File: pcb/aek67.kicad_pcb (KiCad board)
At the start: 2 copper layers, 154 parts, among them J1 AVR-ISP-6, K1 K_GRV, K10 K_LAPP, K11 K_2, K12 K_W, K13 K_S, K14 K_X, K15 K_LALT, K16 K_3, K17 K_E, K18 K_D, K19 K_C, K2 K_TAB, K20 K_4, K21 K_R, K22 K_F, K23 K_V, K24 K_5, K25 K_T, K26 K_G, K27 K_B, K28 K_SPC, K29 K_6, K3 K_CAPS_LOCK, K30 K_Y, K31 K_H, K32 K_N, K33 K_7, K34 K_U, K35 K_J, K36 K_M, K37 K_8, K38 K_I, K39 K_K, K4 K_LSHIFT, K40 K_COMMA, K41 K_9, K42 K_O, K43 K_L, K44 K_DOT, K45 K_0, K46 K_P, K47 K_SEMIC, K48 K_SLASH, K49 K_RALT, K5 K_LCTRL, K50 K_MINUS, K51 K_LBRC, K52 K_QUOTE, K53 K_RAPP, K54 K_EQUAL, K55 K_RBRC, K56 K_ENTER, K57 K_RSHIFT, K58 K_LEFT, K59 K_BACKSPACE, K6 K_1, K60 K_BSLSH, K61 K_UP, K62 K_DOWN, K63 K_PAGE_UP, K64 K_PAGE_DN, K65 K_INSERT, K66 K_DELETE, K67 K_RIGHT, K7 K_Q, K8 K_A, K9 K_Z, SW1 SW_PUSH, U1 PRTR5V0U2X, U2 ATmega32U4-AU, X1 XTAL_GND

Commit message: USB connector & cut lines
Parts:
- C1, C2, C3, C4, C5, C6, C7, F1, R1, R2, R3, R4, R5, R6, SW1, U1, U2, USB1, X1: moved to B.Cu
- moved R6 234.7 mm to (225.0, 110.0), turned to 90 degrees
- moved F1 233.6 mm to (176.9, 33.0), turned to 270 degrees
- moved USB1 230.4 mm to (172.9, 15.1)
- moved U2 228.6 mm to (215.0, 105.0)
- moved R5 226.7 mm to (172.9, 32.9), turned to 90 degrees
- moved R2 217.4 mm to (169.0, 27.5), turned to 90 degrees
- moved U1 215.7 mm to (173.0, 27.5), turned to 90 degrees
- moved SW1 215.6 mm to (195.0, 105.0), turned to 180 degrees
- moved R1 215.0 mm to (177.0, 27.5), turned to 90 degrees
- moved R4 211.8 mm to (169.5, 32.9), turned to 90 degrees
- moved C6 208.8 mm to (220.0, 120.0), turned to 270 degrees
- moved C5 206.2 mm to (210.0, 120.0), turned to 270 degrees
- moved C3 205.1 mm to (202.5, 100.0)
- moved X1 202.8 mm to (215.0, 120.0)
- moved C7 202.0 mm to (202.5, 115.0), turned to 180 degrees
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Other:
- board outline added: 304.8 x 100.4 mm

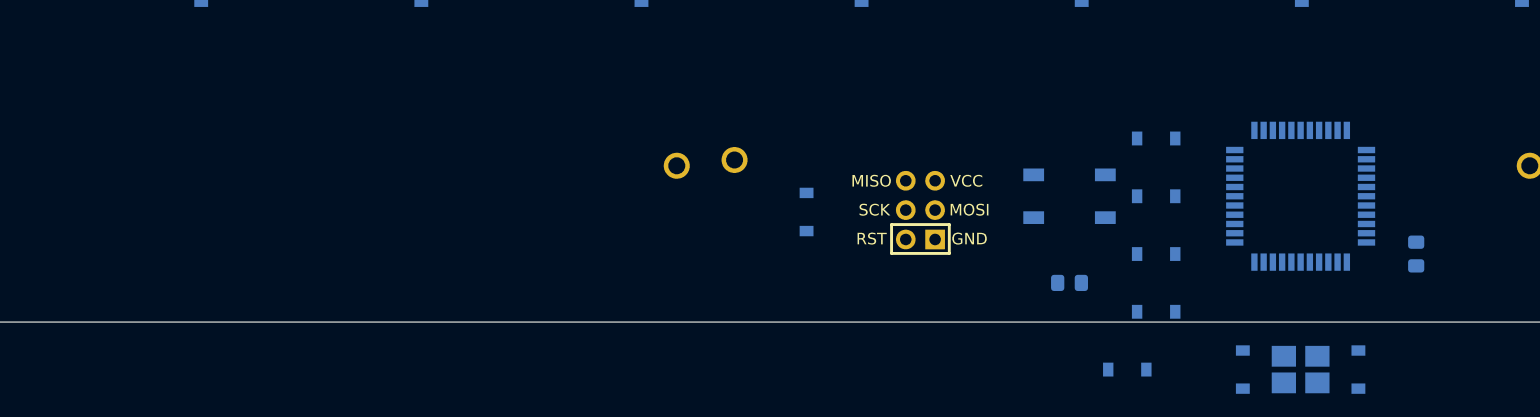
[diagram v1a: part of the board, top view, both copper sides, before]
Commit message: position all elements inside PCB
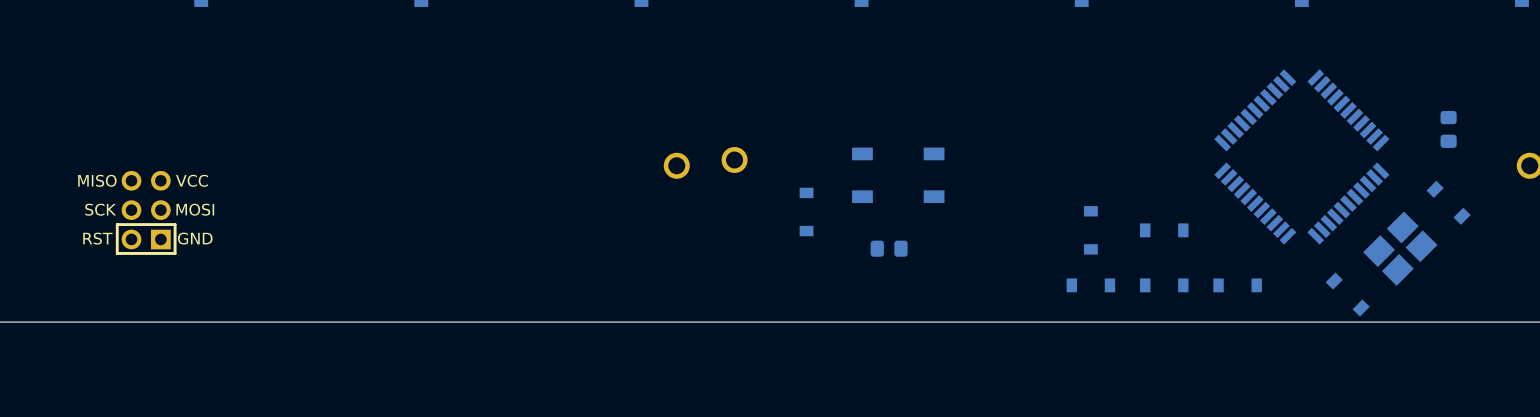
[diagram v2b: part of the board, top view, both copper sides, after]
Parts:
- moved J1 67.0 mm to (115.1, 106.2)
- moved C6 16.4 mm to (227.8, 105.6), turned to 315 degrees
- moved R3 15.9 mm to (179.4, 109.5)
- moved SW1 14.9 mm to (180.2, 103.2)
- moved C3 13.9 mm to (196.8, 112.7)
- moved X1 13.6 mm to (223.6, 109.5), turned to 45 degrees
- moved C1 12.5 mm to (196.8, 108.0), turned to 90 degrees
- moved C5 11.2 mm to (219.1, 113.5), turned to 315 degrees
- moved R6 11.1 mm to (227.8, 99.2)
- moved C7 7.41 mm to (209.6, 112.7)
- moved U2 3.40 mm to (215.1, 101.6), turned to 45 degrees
- moved C2 3.03 mm to (203.2, 108.0)
- moved C4 2.80 mm to (203.2, 112.7)

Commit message: routed switches vertical & diodes
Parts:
- moved J1 31.8 mm to (146.8, 106.4)
- moved C6 24.2 mm to (204.5, 99.0), turned to 135 degrees
- moved C5 22.9 mm to (212.0, 91.8), turned to 135 degrees
- moved X1 21.0 mm to (208.2, 95.2), turned to 225 degrees
- moved R3 10.9 mm to (189.8, 106.2), turned to 270 degrees
- moved R6 8.33 mm to (230.0, 107.2)
- moved C1 8.09 mm to (190.0, 112.2), turned to 270 degrees
- moved C2 6.94 mm to (197.8, 112.2), turned to 270 degrees
- moved R4 6.65 mm to (174.4, 37.4)
- moved R5 4.71 mm to (171.5, 37.4)
- moved U2 4.63 mm to (218.5, 104.8)
- moved C7 4.32 mm to (205.2, 112.2), turned to 270 degrees
- moved U1 4.00 mm to (172.8, 31.5), turned to 270 degrees
- moved SW1 3.70 mm to (182.2, 106.2)
- moved C3 2.89 mm to (194.0, 112.2), turned to 270 degrees
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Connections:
- C1 pad 2: +5V -> GND
- C2 pad 2: +5V -> GND
- C3 pad 2: +5V -> GND
- C4 pad 2: +5V -> GND
- C5 pad 2: Net-(C5-Pad2) -> GND
- C6 pad 2: Net-(C5-Pad2) -> GND
- C7 pad 2: +5V -> GND
- J1 pad 6: +5V -> GND
- K53 pad 1: Net-(K53-Pad1) -> col11
- R1 pad 1: +5V -> GND
- R2 pad 2: +5V -> GND
- R6 pad 1: +5V -> GND
- U1 pad 1: +5V -> GND
- U2 pad 15: +5V -> GND
- U2 pad 23: +5V -> GND
- U2 pad 35: +5V -> GND
- U2 pad 43: +5V -> GND
- U2 pad 5: +5V -> GND
- USB1 pad 1: +5V -> GND
- USB1 pad 12: +5V -> GND
- USB1 pad 13: +5V -> GND
- X1 pad 3: Net-(C5-Pad2) -> GND
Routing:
- net GND: track 0.00 -> 178.0 mm
- net col5: track 0.00 -> 100.4 mm
- net col12: track 0.00 -> 97.8 mm
- net SCLK: track 0.00 -> 94.1 mm
- net Net-(R5-Pad1): track 0.00 -> 92.5 mm
- net Net-(R4-Pad1): track 0.00 -> 91.6 mm
- net col2: track 0.00 -> 90.3 mm
- net col10: track 0.00 -> 89.0 mm
- net +5V: track 0.00 -> 84.7 mm, vias 0 -> 12
- net col13: track 0.00 -> 84.5 mm
- net col0: track 0.00 -> 84.1 mm
- net col11: track 0.00 -> 83.8 mm
- net col14: track 0.00 -> 77.1 mm
- net col4: track 0.00 -> 69.4 mm
- net col3: track 0.00 -> 68.1 mm
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- added copper zone on B.Cu, net GND
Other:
- net class Power added: clearance 0.2, trace_width 0.381, via_dia 0.8, via_drill 0.4

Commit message: row0
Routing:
- net row0: track 0.00 -> 347.2 mm, vias 0 -> 16
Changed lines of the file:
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@@
     (thickness 1.6)
     (drawings 14)
-    (tracks 534)
+    (tracks 613)
     (zones 0)
     (modules 154)
@@
   (segment (start 35.5125 28.5125) (end 38.1 28.5125) (width 0.25) (layer B.Cu) (net 5))
   (segment (start 32.6625 25.6625) (end 35.5125 28.5125) (width 0.25) (layer B.Cu) (net 5))
+  (segment (start 36.5 33.2625) (end 36.5 34.75) (width 0.25) (layer B.Cu) (net 6))
+  (segment (start 37.95 31.8125) (end 36.5 33.2625) (width 0.25) (layer B.Cu) (net 6))
+  (via (at 36.5 34.75) (size 0.8) (drill 0.4) (layers F.Cu B.Cu) (net 6))
+  (segment (start 38.1 31.8125) (end 37.95 31.8125) (width 0.25) (layer B.Cu) (net 6))
+  (via (at 56.25 34.75) (size 0.8) (drill 0.4) (layers F.Cu B.Cu) (net 6))
+  (segment (start 36.5 34.75) (end 56.25 34.75) (width 0.25) (layer F.Cu) (net 6))
+  (segment (start 57.09375 31.8125) (end 57.94375 31.8125) (width 0.25) (layer B.Cu) (net 6))
+  (segment (start 56.25 32.65625) (end 57.09375 31.8125) (width 0.25) (layer B.Cu) (net 6))
+  (segment (start 56.25 34.75) (end 56.25 32.65625) (width 0.25) (layer B.Cu) (net 6))
+  (via (at 74.75 34.75) (size 0.8) (drill 0.4) (layers F.Cu B.Cu) (net 6))
+  (segment (start 56.25 34.75) (end 74.75 34.75) (width 0.25) (layer F.Cu) (net 6))
+  (segment (start 76.14375 31.8125) (end 76.99375 31.8125) (width 0.25) (layer B.Cu) (net 6))
+  (segment (start 74.75 33.20625) (end 76.14375 31.8125) (width 0.25) (layer B.Cu) (net 6))
+  (segment (start 74.75 34.75) (end 74.75 33.20625) (width 0.25) (layer B.Cu) (net 6))
+  (via (at 94 34.75) (size 0.8) (drill 0.4) (layers F.Cu B.Cu) (net 6))
+  (segment (start 74.75 34.75) (end 94 34.75) (width 0.25) (layer F.Cu) (net 6))
+  (segment (start 95.19375 31.8125) (end 96.04375 31.8125) (width 0.25) (layer B.Cu) (net 6))
+  (segment (start 94 33.00625) (end 95.19375 31.8125) (width 0.25) (layer B.Cu) (net 6))
+  (segment (start 94 34.75) (end 94 33.00625) (width 0.25) (layer B.Cu) (net 6))
+  (segment (start 94 34.75) (end 112.5 34.75) (width 0.25) (layer F.Cu) (net 6))
+  (segment (start 112.5 34.75) (end 112.75 34.75) (width 0.25) (layer F.Cu) (net 6))
+  (via (at 112.5 34.75) (size 0.8) (drill 0.4) (layers F.Cu B.Cu) (net 6))
+  (segment (start 112.5 34.75) (end 112.5 32.75) (width 0.25) (layer B.Cu) (net 6))
+  (segment (start 113.4375 31.8125) (end 115.09375 31.8125) (width 0.25) (layer B.Cu) (net 6))
+  (segment (start 112.5 32.75) (end 113.4375 31.8125) (width 0.25) (layer B.Cu) (net 6))
+  (via (at 131.25 34.75) (size 0.8) (drill 0.4) (layers F.Cu B.Cu) (net 6))
+  (segment (start 112.5 34.75) (end 131.25 34.75) (width 0.25) (layer F.Cu) (net 6))
+  (segment (start 131.25 34.75) (end 131.25 33.5) (width 0.25) (layer B.Cu) (net 6))
+  (segment (start 132.9375 31.8125) (end 134.14375 31.8125) (width 0.25) (layer B.Cu) (net 6))
+  (segment (start 131.25 33.5) (end 132.9375 31.8125) (width 0.25) (layer B.Cu) (net 6))
+  (via (at 150.5 34.75) (size 0.8) (drill 0.4) (layers F.Cu B.Cu) (net 6))
+  (segment (start 131.25 34.75) (end 150.5 34.75) (width 0.25) (layer F.Cu) (net 6))
+  (segment (start 150.5 34.75) (end 150.5 32.75) (width 0.25) (layer B.Cu) (net 6))
+  (segment (start 151.4375 31.8125) (end 153.19375 31.8125) (width 0.25) (layer B.Cu) (net 6))
+  (segment (start 150.5 32.75) (end 151.4375 31.8125) (width 0.25) (layer B.Cu) (net 6))
+  (segment (start 153.19375 31.8125) (end 156.5 31.8125) (width 0.25) (layer B.Cu) (net 6))
+  (segment (start 156.5 31.8125) (end 157.8125 31.8125) (width 0.25) (layer B.Cu) (net 6))
+  (segment (start 157.8125 31.8125) (end 158.75 32.75) (width 0.25) (layer B.Cu) (net 6))
+  (segment (start 158.75 32.75) (end 158.75 34.75) (width 0.25) (layer B.Cu) (net 6))
+  (via (at 158.75 34.75) (size 0.8) (drill 0.4) (layers F.Cu B.Cu) (net 6))
+  (via (at 188.25 34.75) (size 0.8) (drill 0.4) (layers F.Cu B.Cu) (net 6))
+  (segment (start 158.75 34.75) (end 188.25 34.75) (width 0.25) (layer F.Cu) (net 6))
+  (segment (start 188.25 34.75) (end 188.25 32.75) (width 0.25) (layer B.Cu) (net 6))
+  (segment (start 189.35 31.65) (end 191 31.65) (width 0.25) (layer B.Cu) (net 6))
+  (segment (start 188.25 32.75) (end 189.35 31.65) (width 0.25) (layer B.Cu) (net 6))
+  (segment (start 188.25 34.75) (end 207.5 34.75) (width 0.25) (layer F.Cu) (net 6))
+  (via (at 207.5 34.75) (size 0.8) (drill 0.4) (layers F.Cu B.Cu) (net 6))
+  (segment (start 207.5 34.75) (end 207.5 33.25) (width 0.25) (layer B.Cu) (net 6))
+  (segment (start 208.9375 31.8125) (end 210.34375 31.8125) (width 0.25) (layer B.Cu) (net 6))
+  (segment (start 207.5 33.25) (end 208.9375 31.8125) (width 0.25) (layer B.Cu) (net 6))
+  (segment (start 207.5 34.75) (end 224 34.75) (width 0.25) (layer F.Cu) (net 6))
+  (segment (start 224 34.75) (end 226 34.75) (width 0.25) (layer F.Cu) (net 6))
+  (via (at 226 34.75) (size 0.8) (drill 0.4) (layers F.Cu B.Cu) (net 6))
+  (segment (start 227.4375 31.8125) (end 229.39375 31.8125) (width 0.25) (layer B.Cu) (net 6))
+  (segment (start 226 33.25) (end 227.4375 31.8125) (width 0.25) (layer B.Cu) (net 6))
+  (segment (start 226 34.75) (end 226 33.25) (width 0.25) (layer B.Cu) (net 6))
+  (segment (start 226 34.75) (end 242.25 34.75) (width 0.25) (layer F.Cu) (net 6))
+  (segment (start 242.25 34.75) (end 246 34.75) (width 0.25) (layer F.Cu) (net 6))
+  (via (at 246 34.75) (size 0.8) (drill 0.4) (layers F.Cu B.Cu) (net 6))
+  (via (at 246 34.75) (size 0.8) (drill 0.4) (layers F.Cu B.Cu) (net 6))
+  (segment (start 246 34.184315) (end 246 34.75) (width 0.25) (layer B.Cu) (net 6))
+  (segment (start 246 33.40625) (end 246 34.184315) (width 0.25) (layer B.Cu) (net 6))
+  (segment (start 247.59375 31.8125) (end 246 33.40625) (width 0.25) (layer B.Cu) (net 6))
+  (segment (start 248.44375 31.8125) (end 247.59375 31.8125) (width 0.25) (layer B.Cu) (net 6))
+  (via (at 265 34.75) (size 0.8) (drill 0.4) (layers F.Cu B.Cu) (net 6))
+  (segment (start 246 34.75) (end 265 34.75) (width 0.25) (layer F.Cu) (net 6))
+  (segment (start 265 34.75) (end 265 33.25) (width 0.25) (layer B.Cu) (net 6))
+  (segment (start 266.4375 31.8125) (end 267.49375 31.8125) (width 0.25) (layer B.Cu) (net 6))
+  (segment (start 265 33.25) (end 266.4375 31.8125) (width 0.25) (layer B.Cu) (net 6))
+  (segment (start 265 34.75) (end 295 34.75) (width 0.25) (layer F.Cu) (net 6))
+  (via (at 295 34.75) (size 0.8) (drill 0.4) (layers F.Cu B.Cu) (net 6))
+  (segment (start 295 34.75) (end 295 33.25) (width 0.25) (layer B.Cu) (net 6))
+  (segment (start 296.4375 31.8125) (end 297.65625 31.8125) (width 0.25) (layer B.Cu) (net 6))
+  (segment (start 295 33.25) (end 296.4375 31.8125) (width 0.25) (layer B.Cu) (net 6))
+  (segment (start 295 34.75) (end 316 34.75) (width 0.25) (layer F.Cu) (net 6))
+  (via (at 317.5 33.25) (size 0.8) (drill 0.4) (layers F.Cu B.Cu) (net 6))
+  (segment (start 316 34.75) (end 317.5 33.25) (width 0.25) (layer F.Cu) (net 6))
+  (segment (start 322.1125 33.25) (end 322.2625 33.4) (width 0.25) (layer B.Cu) (net 6))
+  (segment (start 317.5 33.25) (end 322.1125 33.25) (width 0.25) (layer B.Cu) (net 6))
   (segment (start 43.65625 46.8625) (end 43.65625 47.5625) (width 0.25) (layer B.Cu) (net 7))
   (segment (start 41.50625 44.7125) (end 43.65625 46.8625) (width 0.25) (layer B.Cu) (net 7))

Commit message: re-annotated everything in line instead of column
which is more clear for the matrix
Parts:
- renumbered D41 to D10, D45 to D11, D50 to D12, D54 to D13, D59 to D14, D63 to D15, D2 to D16, D7 to D17, D12 to D18, D17 to D19, D6 to D2, D21 to D20, D25 to D21, D30 to D22, D34 to D23, D38 to D24, D42 to D25, D46 to D26, D51 to D27, D55 to D28, D60 to D29, D11 to D3, D64 to D30, D3 to D31, D8 to D32, D13 to D33, D18 to D34, D22 to D35, D26 to D36, D31 to D37, D35 to D38, D16 to D4, D43 to D40, D47 to D41, D52 to D42, D56 to D43, D65 to D44, D4 to D45, D9 to D46, D14 to D47, D19 to D48, D23 to D49, D20 to D5, D27 to D50, D32 to D51, D36 to D52, D40 to D53, D44 to D54, D48 to D55, D57 to D56, D61 to D57, D66 to D58, D5 to D59, D24 to D6, D10 to D60, D15 to D61, D28 to D62, D49 to D63, D53 to D64, D58 to D65, D62 to D66, D29 to D7, D33 to D8, D37 to D9, K41 to K10, K45 to K11, K50 to K12, K54 to K13, K59 to K14, K63 to K15, K2 to K16, K7 to K17, K12 to K18, K17 to K19, K6 to K2, K21 to K20, K25 to K21, K30 to K22, K34 to K23, K38 to K24, K42 to K25, K46 to K26, K51 to K27, K55 to K28, K60 to K29, K11 to K3, K64 to K30, K3 to K31, K8 to K32, K13 to K33, K18 to K34, K22 to K35, K26 to K36, K31 to K37, K35 to K38, K16 to K4, K43 to K40, K47 to K41, K52 to K42, K56 to K43, K65 to K44, K4 to K45, K9 to K46, K14 to K47, K19 to K48, K23 to K49, K20 to K5, K27 to K50, K32 to K51, K36 to K52, K40 to K53, K44 to K54, K48 to K55, K57 to K56, K61 to K57, K66 to K58, K5 to K59, K24 to K6, K10 to K60, K15 to K61, K28 to K62, K49 to K63, K53 to K64, K58 to K65, K62 to K66, K29 to K7, K33 to K8, K37 to K9, R3 to R1, R4 to R2, R5 to R3, R6 to R4, R1 to R5, R2 to R6, U2 to U1, U1 to U2

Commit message: row1
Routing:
- net row1: track 0.00 -> 405.2 mm, vias 0 -> 15
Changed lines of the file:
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@@
     (thickness 1.6)
     (drawings 14)
-    (tracks 613)
+    (tracks 701)
     (zones 0)
     (modules 154)
     (nets 110)
   )
-  (page A4)
+  (page A3)
   (layers
     (0 F.Cu signal)
@@
   (segment (start 55.79375 25.6625) (end 57.94375 27.8125) (width 0.25) (layer B.Cu) (net 7))
   (segment (start 51.7125 25.6625) (end 55.79375 25.6625) (width 0.25) (layer B.Cu) (net 7))
+  (segment (start 42.80625 50.8625) (end 41 52.66875) (width 0.25) (layer B.Cu) (net 8))
+  (segment (start 43.65625 50.8625) (end 42.80625 50.8625) (width 0.25) (layer B.Cu) (net 8))
+  (via (at 41 57.5) (size 0.8) (drill 0.4) (layers F.Cu B.Cu) (net 8))
+  (via (at 64.5 57.5) (size 0.8) (drill 0.4) (layers F.Cu B.Cu) (net 8))
+  (segment (start 41 57.5) (end 64.5 57.5) (width 0.25) (layer F.Cu) (net 8))
+  (segment (start 65.8875 50.8625) (end 67.46875 50.8625) (width 0.25) (layer B.Cu) (net 8))
+  (segment (start 64.5 52.25) (end 65.8875 50.8625) (width 0.25) (layer B.Cu) (net 8))
+  (via (at 83.75 57.5) (size 0.8) (drill 0.4) (layers F.Cu B.Cu) (net 8))
+  (segment (start 64.5 57.5) (end 83.75 57.5) (width 0.25) (layer F.Cu) (net 8))
+  (segment (start 84.8875 50.8625) (end 86.51875 50.8625) (width 0.25) (layer B.Cu) (net 8))
+  (segment (start 83.75 52) (end 84.8875 50.8625) (width 0.25) (layer B.Cu) (net 8))
+  (segment (start 83.75 57.5) (end 103 57.5) (width 0.25) (layer F.Cu) (net 8))
+  (via (at 103 57.5) (size 0.8) (drill 0.4) (layers F.Cu B.Cu) (net 8))
+  (segment (start 104.3875 50.8625) (end 105.56875 50.8625) (width 0.25) (layer B.Cu) (net 8))
+  (segment (start 103 52.25) (end 104.3875 50.8625) (width 0.25) (layer B.Cu) (net 8))
+  (segment (start 103 57.5) (end 121 57.5) (width 0.25) (layer F.Cu) (net 8))
+  (via (at 121 57.5) (size 0.8) (drill 0.4) (layers F.Cu B.Cu) (net 8))
+  (segment (start 122.6375 50.8625) (end 124.61875 50.8625) (width 0.25) (layer B.Cu) (net 8))
+  (segment (start 121 52.5) (end 122.6375 50.8625) (width 0.25) (layer B.Cu) (net 8))
+  (via (at 139.75 57.5) (size 0.8) (drill 0.4) (layers F.Cu B.Cu) (net 8))
+  (segment (start 121 57.5) (end 139.75 57.5) (width 0.25) (layer F.Cu) (net 8))
+  (segment (start 141.3875 50.8625) (end 143.66875 50.8625) (width 0.25) (layer B.Cu) (net 8))
+  (segment (start 139.75 52.5) (end 141.3875 50.8625) (width 0.25) (layer B.Cu) (net 8))
+  (segment (start 139.75 57.5) (end 159 57.5) (width 0.25) (layer F.Cu) (net 8))
+  (via (at 159 57.5) (size 0.8) (drill 0.4) (layers F.Cu B.Cu) (net 8))
+  (segment (start 160.1375 50.8625) (end 162.71875 50.8625) (width 0.25) (layer B.Cu) (net 8))
+  (segment (start 159 52) (end 160.1375 50.8625) (width 0.25) (layer B.Cu) (net 8))
+  (via (at 179.5 57.5) (size 0.8) (drill 0.4) (layers F.Cu B.Cu) (net 8))
+  (segment (start 159 57.5) (end 179.5 57.5) (width 0.25) (layer F.Cu) (net 8))
+  (segment (start 180.91875 50.8625) (end 181.76875 50.8625) (width 0.25) (layer B.Cu) (net 8))
+  (segment (start 179.5 52.28125) (end 180.91875 50.8625) (width 0.25) (layer B.Cu) (net 8))
+  (segment (start 179.5 57.5) (end 199 57.5) (width 0.25) (layer F.Cu) (net 8))
+  (via (at 199 57.5) (size 0.8) (drill 0.4) (layers F.Cu B.Cu) (net 8))
+  (segment (start 199.6375 50.8625) (end 200.81875 50.8625) (width 0.25) (layer B.Cu) (net 8))
+  (segment (start 199 51.5) (end 199.6375 50.8625) (width 0.25) (layer B.Cu) (net 8))
+  (segment (start 199 57.5) (end 218.25 57.5) (width 0.25) (layer F.Cu) (net 8))
+  (via (at 218.25 57.5) (size 0.8) (drill 0.4) (layers F.Cu B.Cu) (net 8))
+  (segment (start 219.86875 55.88125) (end 219.86875 50.8625) (width 0.25) (layer B.Cu) (net 8))
+  (segment (start 218.25 57.5) (end 219.86875 55.88125) (width 0.25) (layer B.Cu) (net 8))
+  (segment (start 41 57.5) (end 41 53.5) (width 0.25) (layer B.Cu) (net 8))
+  (segment (start 41 53.5) (end 41 53.75) (width 0.25) (layer B.Cu) (net 8))
+  (segment (start 41 52.66875) (end 41 53.5) (width 0.25) (layer B.Cu) (net 8))
+  (segment (start 64.5 57.5) (end 64.5 53.5) (width 0.25) (layer B.Cu) (net 8))
+  (segment (start 64.5 53.5) (end 64.5 52.25) (width 0.25) (layer B.Cu) (net 8))
+  (segment (start 64.5 53.75) (end 64.5 53.5) (width 0.25) (layer B.Cu) (net 8))
+  (segment (start 83.75 57.5) (end 83.75 53.25) (width 0.25) (layer B.Cu) (net 8))
+  (segment (start 83.75 53.25) (end 83.75 52) (width 0.25) (layer B.Cu) (net 8))
+  (segment (start 83.75 53.75) (end 83.75 53.25) (width 0.25) (layer B.Cu) (net 8))
+  (segment (start 103 57.5) (end 103 53.25) (width 0.25) (layer B.Cu) (net 8))
+  (segment (start 103 53.25) (end 103 52.25) (width 0.25) (layer B.Cu) (net 8))
+  (segment (start 103 53.75) (end 103 53.25) (width 0.25) (layer B.Cu) (net 8))
+  (segment (start 121 57.5) (end 121 53.25) (width 0.25) (layer B.Cu) (net 8))
+  (segment (start 121 53.25) (end 121 52.5) (width 0.25) (layer B.Cu) (net 8))
+  (segment (start 121 53.75) (end 121 53.25) (width 0.25) (layer B.Cu) (net 8))
+  (segment (start 139.75 57.5) (end 139.75 53.25) (width 0.25) (layer B.Cu) (net 8))
+  (segment (start 139.75 53.25) (end 139.75 52.5) (width 0.25) (layer B.Cu) (net 8))
+  (segment (start 139.75 53.75) (end 139.75 53.25) (width 0.25) (layer B.Cu) (net 8))
+  (segment (start 159 57.5) (end 159 52.5) (width 0.25) (layer B.Cu) (net 8))
+  (segment (start 159 52.5) (end 159 52) (width 0.25) (layer B.Cu) (net 8))
+  (segment (start 159 53.75) (end 159 52.5) (width 0.25) (layer B.Cu) (net 8))
+  (segment (start 179.5 57.5) (end 179.5 52.75) (width 0.25) (layer B.Cu) (net 8))
+  (segment (start 179.5 52.75) (end 179.5 52.28125) (width 0.25) (layer B.Cu) (net 8))
+  (segment (start 179.5 53.75) (end 179.5 52.75) (width 0.25) (layer B.Cu) (net 8))
+  (segment (start 199 57.5) (end 199 53.25) (width 0.25) (layer B.Cu) (net 8))
+  (segment (start 199 53.25) (end 199 51.5) (width 0.25) (layer B.Cu) (net 8))
+  (segment (start 199 53.75) (end 199 53.25) (width 0.25) (layer B.Cu) (net 8))
+  (segment (start 218.25 57.5) (end 237.5 57.5) (width 0.25) (layer F.Cu) (net 8))
+  (via (at 237.5 57.5) (size 0.8) (drill 0.4) (layers F.Cu B.Cu) (net 8))
+  (segment (start 238.91875 56.08125) (end 238.91875 50.8625) (width 0.25) (layer B.Cu) (net 8))
+  (segment (start 237.5 57.5) (end 238.91875 56.08125) (width 0.25) (layer B.Cu) (net 8))
+  (via (at 256.75 57.5) (size 0.8) (drill 0.4) (layers F.Cu B.Cu) (net 8))
+  (segment (start 237.5 57.5) (end 256.75 57.5) (width 0.25) (layer F.Cu) (net 8))
+  (segment (start 256.75 57.5) (end 258 56.25) (width 0.25) (layer B.Cu) (net 8))
+  (segment (start 257.96875 56.21875) (end 257.96875 50.8625) (width 0.25) (layer B.Cu) (net 8))
+  (segment (start 258 56.25) (end 257.96875 56.21875) (width 0.25) (layer B.Cu) (net 8))
+  (via (at 275.75 57.5) (size 0.8) (drill 0.4) (layers F.Cu B.Cu) (net 8))
+  (segment (start 256.75 57.5) (end 275.75 57.5) (width 0.25) (layer F.Cu) (net 8))
+  (segment (start 277.01875 56.23125) (end 277.01875 50.8625) (width 0.25) (layer B.Cu) (net 8))
+  (segment (start 275.75 57.5) (end 277.01875 56.23125) (width 0.25) (layer B.Cu) (net 8))
+  (via (at 300.75 57.5) (size 0.8) (drill 0.4) (layers F.Cu B.Cu) (net 8))
+  (segment (start 275.75 57.5) (end 300.75 57.5) (width 0.25) (layer F.Cu) (net 8))
+  (segment (start 300.75 50.94375) (end 300.83125 50.8625) (width 0.25) (layer B.Cu) (net 8))
+  (segment (start 300.75 57.5) (end 300.75 50.94375) (width 0.25) (layer B.Cu) (net 8))
+  (via (at 320 57.5) (size 0.8) (drill 0.4) (layers F.Cu B.Cu) (net 8))
+  (segment (start 300.75 57.5) (end 320 57.5) (width 0.25) (layer F.Cu) (net 8))
+  (segment (start 321.4125 52.45) (end 322.2625 52.45) (width 0.25) (layer B.Cu) (net 8))
+  (segment (start 320 53.8625) (end 321.4125 52.45) (width 0.25) (layer B.Cu) (net 8))
+  (segment (start 320 57.5) (end 320 53.8625) (width 0.25) (layer B.Cu) (net 8))
   (segment (start 67.46875 46.8625) (end 67.46875 47.5625) (width 0.25) (layer B.Cu) (net 26))
   (segment (start 65.31875 44.7125) (end 67.46875 46.8625) (width 0.25) (layer B.Cu) (net 26))

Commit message: row2
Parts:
- moved D41 1.77 mm to (243.5, 68.3)
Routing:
- net row2: track 0.00 -> 373.0 mm, vias 0 -> 14
- net row0: track 347.2 -> 378.1 mm
- net Net-(D41-Pad2): track 9.41 -> 8.68 mm
